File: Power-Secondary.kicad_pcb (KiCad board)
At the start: 2 copper layers, 83 x 60 mm, 35 parts, among them J1 SUPP PWR MON, J2 SUPP PWR 1, J3 SUPP PWR 2, J4 DCDC SUPPLY, J5 FUSE +12V, Q1A1 SUP90P06-PCHANNEL-MOSFET, Q2B1 SUP90P06-PCHANNEL-MOSFET, U1 Opamp_Dual

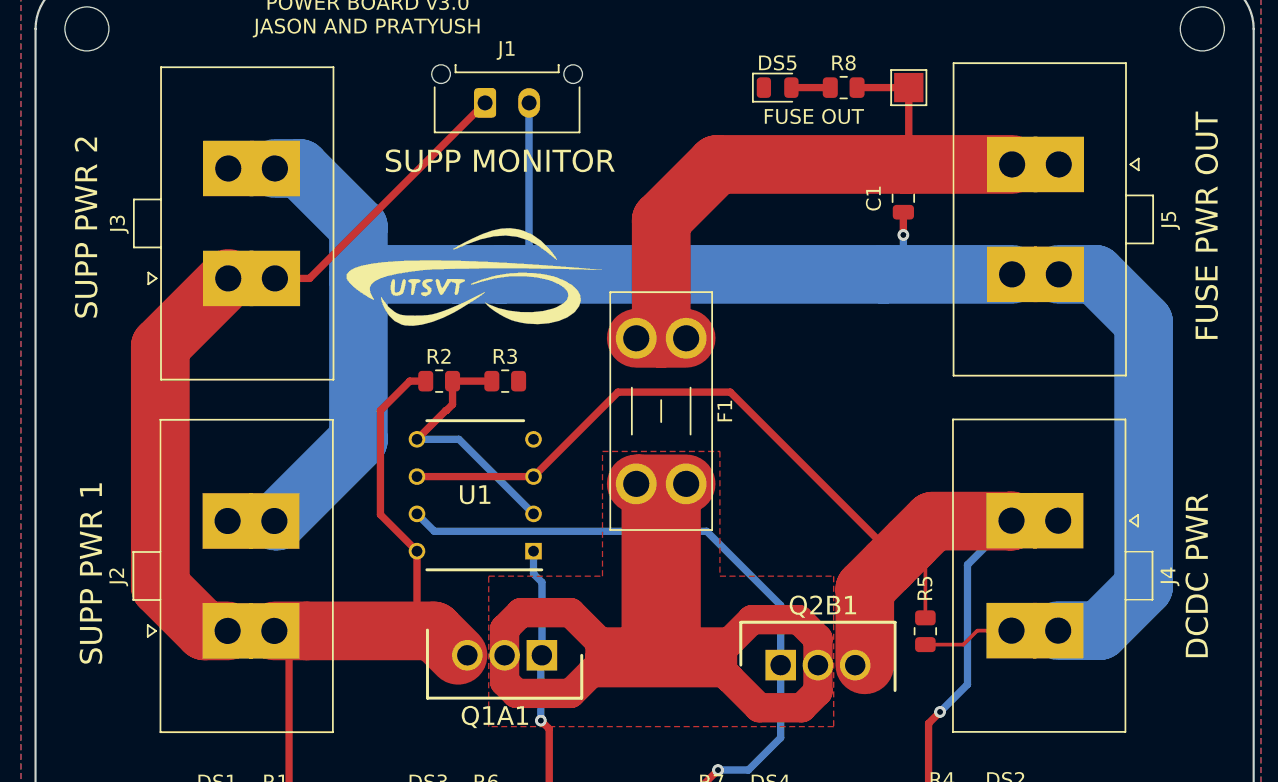
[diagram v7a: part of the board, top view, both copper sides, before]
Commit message: updated gerbers and fixed clearence issues
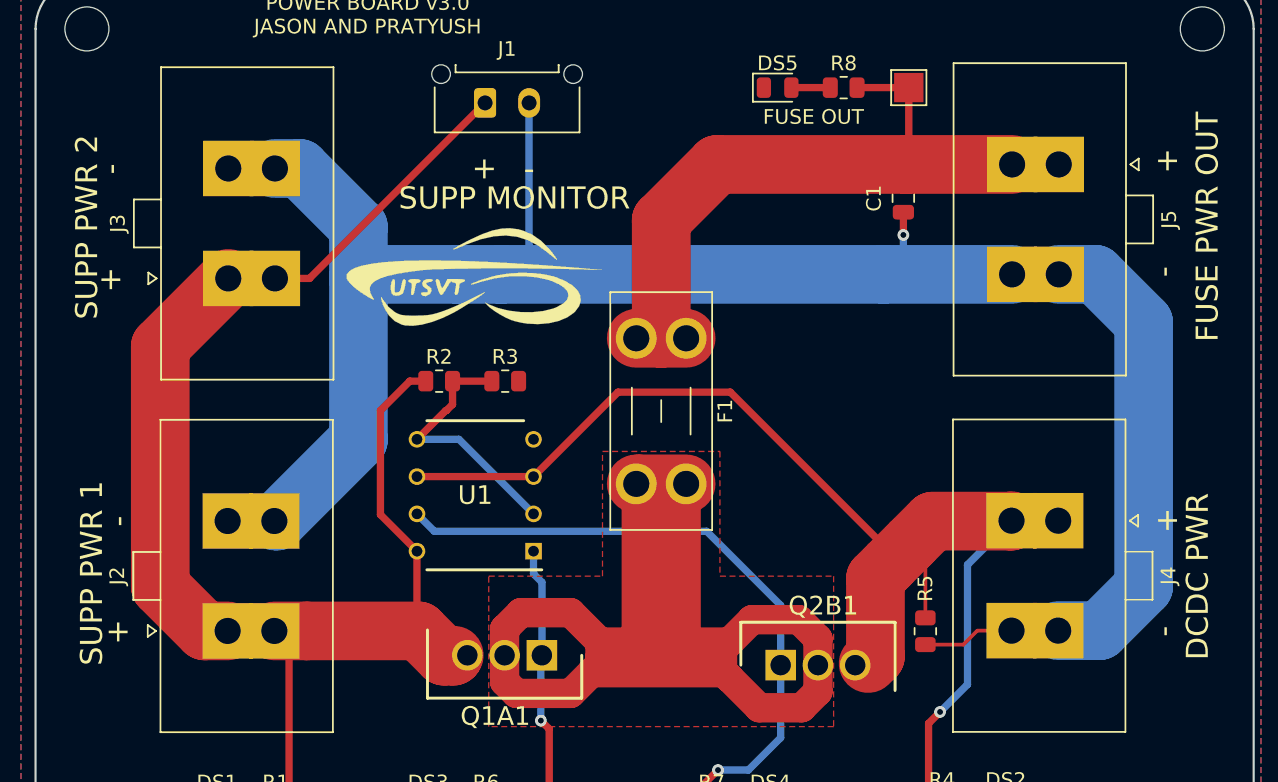
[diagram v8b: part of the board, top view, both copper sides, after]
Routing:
- net SUPP_PWR: track 97.4 -> 100.1 mm
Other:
- board text added: "+"
- board text added: "-"
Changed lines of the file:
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@@
       (layerselection 0x00010fc_ffffffff)
       (disableapertmacros false)
-      (usegerberextensions true)
+      (usegerberextensions false)
       (usegerberattributes false)
       (usegerberadvancedattributes false)
@@
       (psa4output false)
       (plotreference true)
-      (plotvalue false)
+      (plotvalue true)
       (plotinvisibletext false)
       (sketchpadsonfab false)
-      (subtractmaskfromsilk true)
+      (subtractmaskfromsilk false)
       (outputformat 1)
       (mirror false)
@@
     (pad "" np_thru_hole circle (at -3 -1.96) (size 1.27 1.27) (drill 1.27) (layers *.Cu *.Mask))
     (pad "" np_thru_hole circle (at 6 -1.96) (size 1.27 1.27) (drill 1.27) (layers *.Cu *.Mask))
-    (pad "1" thru_hole roundrect (at 0 0) (size 1.5 2.02) (drill 1.02) (layers *.Cu *.Mask) (roundrect_rratio 0.166667)
+    (pad "1" thru_hole roundrect (at 0 0) (size 1.5 2.02) (drill 1.02) (layers *.Cu *.Mask) (roundrect_rratio 0.1666673333)
       (net 8 "SUPP_PWR") (pinfunction "Pin_1") (pintype "passive"))
     (pad "2" thru_hole oval (at 3 0) (size 1.5 2.02) (drill 1.02) (layers *.Cu *.Mask)
@@
     (effects (font (size 1 1) (thickness 0.15)) (justify mirror))
   )
-  (gr_text "SUPP MONITOR" (at 138 80) (layer "F.SilkS")
+  (gr_text "+" (at 137 80.5 270) (layer "F.SilkS")
+    (effects (font (size 1.5 1.5) (thickness 0.3)))
+  )
+  (gr_text "+" (at 183.5 104.5 180) (layer "F.SilkS")
+    (effects (font (size 1.5 1.5) (thickness 0.3)))
+  )
+  (gr_text "SUPP MONITOR" (at 139 82.5) (layer "F.SilkS")
     (effects (font (size 1.5 1.5) (thickness 0.3)))
   )
@@
     (effects (font (size 1 1) (thickness 0.15)))
   )
+  (gr_text "+" (at 183.5 80 180) (layer "F.SilkS")
+    (effects (font (size 1.5 1.5) (thickness 0.3)))
+  )
+  (gr_text "+" (at 111.5 88) (layer "F.SilkS")
+    (effects (font (size 1.5 1.5) (thickness 0.3)))
+  )
+  (gr_text "-" (at 140 80.5) (layer "F.SilkS")
+    (effects (font (size 1.5 1.5) (thickness 0.3)))
+  )
+  (gr_text "-" (at 183.5 112 270) (layer "F.SilkS")
+    (effects (font (size 1.5 1.5) (thickness 0.3)))
+  )
   (gr_text "DCDC PWR" (at 167.87 126.46) (layer "F.SilkS")
     (effects (font (size 1 1) (thickness 0.15)))
   )
+  (gr_text "-" (at 111.5 80.5 90) (layer "F.SilkS")
+    (effects (font (size 1.5 1.5) (thickness 0.3)))
+  )
+  (gr_text "-" (at 112 104.5 90) (layer "F.SilkS")
+    (effects (font (size 1.5 1.5) (thickness 0.3)))
+  )
   (gr_text "DCDC PWR" (at 185.55 108.27 90) (layer "F.SilkS")
     (effects (font (size 1.5 1.5) (thickness 0.3)))
@@
     (effects (font (size 1 1) (thickness 0.15)))
   )
+  (gr_text "-" (at 183.5 87.5 270) (layer "F.SilkS")
+    (effects (font (size 1.5 1.5) (thickness 0.3)))
+  )
   (gr_text "DCDC GATE" (at 152.37 126.46) (layer "F.SilkS")
     (effects (font (size 1 1) (thickness 0.15)))
@@
     (effects (font (size 1 1) (thickness 0.15)))
   )
+  (gr_text "+" (at 112 112) (layer "F.SilkS")
+    (effects (font (size 1.5 1.5) (thickness 0.3)))
+  )
   (segment (start 162.345 74.96) (end 165.87 74.96) (width 0.5) (layer "F.Cu") (net 1))
   (segment (start 148.96 92.04) (end 147.3 92.04) (width 4) (layer "F.Cu") (net 1))
@@
   (segment (start 117.89 111.98) (end 114.87 108.96) (width 4) (layer "F.Cu") (net 8))
   (segment (start 129.87 104.055) (end 129.87 96.96) (width 0.5) (layer "F.Cu") (net 8))
+  (segment (start 134.84 113.7) (end 134.2 113.7) (width 4) (layer "F.Cu") (net 8))
   (segment (start 114.87 108.96) (end 114.87 92.59) (width 4) (layer "F.Cu") (net 8))
-  (segment (start 132.36 110.8395) (end 133.5005 111.98) (width 0.5) (layer "F.Cu") (net 8))
-  (segment (start 124.85 111.98) (end 133.5005 111.98) (width 4) (layer "F.Cu") (net 8))
-  (segment (start 133.5005 111.98) (end 135.1605 113.64) (width 4) (layer "F.Cu") (net 8))
+  (segment (start 134.9 113.64) (end 134.84 113.7) (width 4) (layer "F.Cu") (net 8))
+  (segment (start 134.2 113.7) (end 132.36 111.86) (width 0.5) (layer "F.Cu") (net 8))
   (segment (start 123.645 123.96) (end 123.645 113.185) (width 0.5) (layer "F.Cu") (net 8))
   (segment (start 123.645 123.96) (end 126.87 123.96) (width 0.5) (layer "F.Cu") (net 8))
+  (segment (start 124.85 111.98) (end 132.48 111.98) (width 4) (layer "F.Cu") (net 8))
   (segment (start 122.64 111.98) (end 124.85 111.98) (width 4) (layer "F.Cu") (net 8))
-  (segment (start 132.36 106.545) (end 132.36 110.8395) (width 0.5) (layer "F.Cu") (net 8))
+  (segment (start 132.48 111.98) (end 134.2 113.7) (width 4) (layer "F.Cu") (net 8))
   (segment (start 123.645 113.185) (end 124.85 111.98) (width 0.5) (layer "F.Cu") (net 8))
   (segment (start 114.87 92.59) (end 119.5 87.96) (width 4) (layer "F.Cu") (net 8))
   (segment (start 137 76) (end 125.04 87.96) (width 0.5) (layer "F.Cu") (net 8))
+  (segment (start 135.79 113.64) (end 134.9 113.64) (width 0.5) (layer "F.Cu") (net 8))
   (segment (start 129.87 96.96) (end 131.87 94.96) (width 0.5) (layer "F.Cu") (net 8))
+  (segment (start 132.36 111.86) (end 132.36 106.545) (width 0.5) (layer "F.Cu") (net 8))
   (segment (start 131.87 94.96) (end 132.9575 94.96) (width 0.5) (layer "F.Cu") (net 8))
   (segment (start 132.36 106.545) (end 129.87 104.055) (width 0.5) (layer "F.Cu") (net 8))
   (segment (start 125.04 87.96) (end 122.68 87.96) (width 0.5) (layer "F.Cu") (net 8))
+  (segment (start 163.1 114.2) (end 163.6 113.7) (width 4) (layer "F.Cu") (net 9))
   (segment (start 167 111.0875) (end 167 107) (width 0.25) (layer "F.Cu") (net 9))
   (segment (start 166 106) (end 164.5 107.5) (width 4) (layer "F.Cu") (net 9))
   (segment (start 167.22 118.28) (end 167.22 124.02125) (width 0.5) (layer "F.Cu") (net 9))
-  (segment (start 162.87 109.13) (end 162.87 114.2895) (width 4) (layer "F.Cu") (net 9))
+  (segment (start 163.6 113.7) (end 163.6 108.4) (width 4) (layer "F.Cu") (net 9))
   (segment (start 167.5 104.5) (end 172.84 104.5) (width 4) (layer "F.Cu") (net 9))
   (segment (start 153.71 95.71) (end 146.055 95.71) (width 0.5) (layer "F.Cu") (net 9))
-  (segment (start 162.695 113.835) (end 162.22 114.31) (width 0.5) (layer "F.Cu") (net 9))
   (segment (start 164.5 107.5) (end 164.5 106.5) (width 0.5) (layer "F.Cu") (net 9))
   (segment (start 167 107) (end 166 106) (width 0.25) (layer "F.Cu") (net 9))
   (segment (start 167.5 104.5) (end 166 106) (width 4) (layer "F.Cu") (net 9))
+  (segment (start 162.33 114.2) (end 163.1 114.2) (width 2) (layer "F.Cu") (net 9))
   (segment (start 172.84 104.5) (end 172.87 104.47) (width 4) (layer "F.Cu") (net 9))
   (segment (start 164.5 106.5) (end 153.71 95.71) (width 0.5) (layer "F.Cu") (net 9))
+  (segment (start 163.6 108.4) (end 164.5 107.5) (width 4) (layer "F.Cu") (net 9))
+  (segment (start 162.22 114.31) (end 162.33 114.2) (width 2) (layer "F.Cu") (net 9))
   (segment (start 132.36 101.465) (end 140.3 101.465) (width 0.5) (layer "F.Cu") (net 9))
   (segment (start 167.22 124.02125) (end 164.0175 124.02125) (width 0.5) (layer "F.Cu") (net 9))
   (segment (start 146.055 95.71) (end 140.3 101.465) (width 0.5) (layer "F.Cu") (net 9))
   (segment (start 168 117.5) (end 167.22 118.28) (width 0.5) (layer "F.Cu") (net 9))
-  (segment (start 164.5 107.5) (end 162.87 109.13) (width 4) (layer "F.Cu") (net 9))
   (via (at 168 117.5) (size 0.8) (drill 0.4) (layers "F.Cu" "B.Cu") (net 9))
   (segment (start 169.87 107.47) (end 172.87 104.47) (width 0.5) (layer "B.Cu") (net 9))
@@
     (connect_pads (clearance 0.508))
     (min_thickness 0.254) (filled_areas_thickness no)
-    (fill yes (thermal_gap 0.508) (thermal_bridge_width 0.508))
+    (fill yes (thermal_gap 0.508) (thermal_bridge_width 2))
     (polygon
       (pts
